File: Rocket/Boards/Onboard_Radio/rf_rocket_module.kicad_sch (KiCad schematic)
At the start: 13 parts

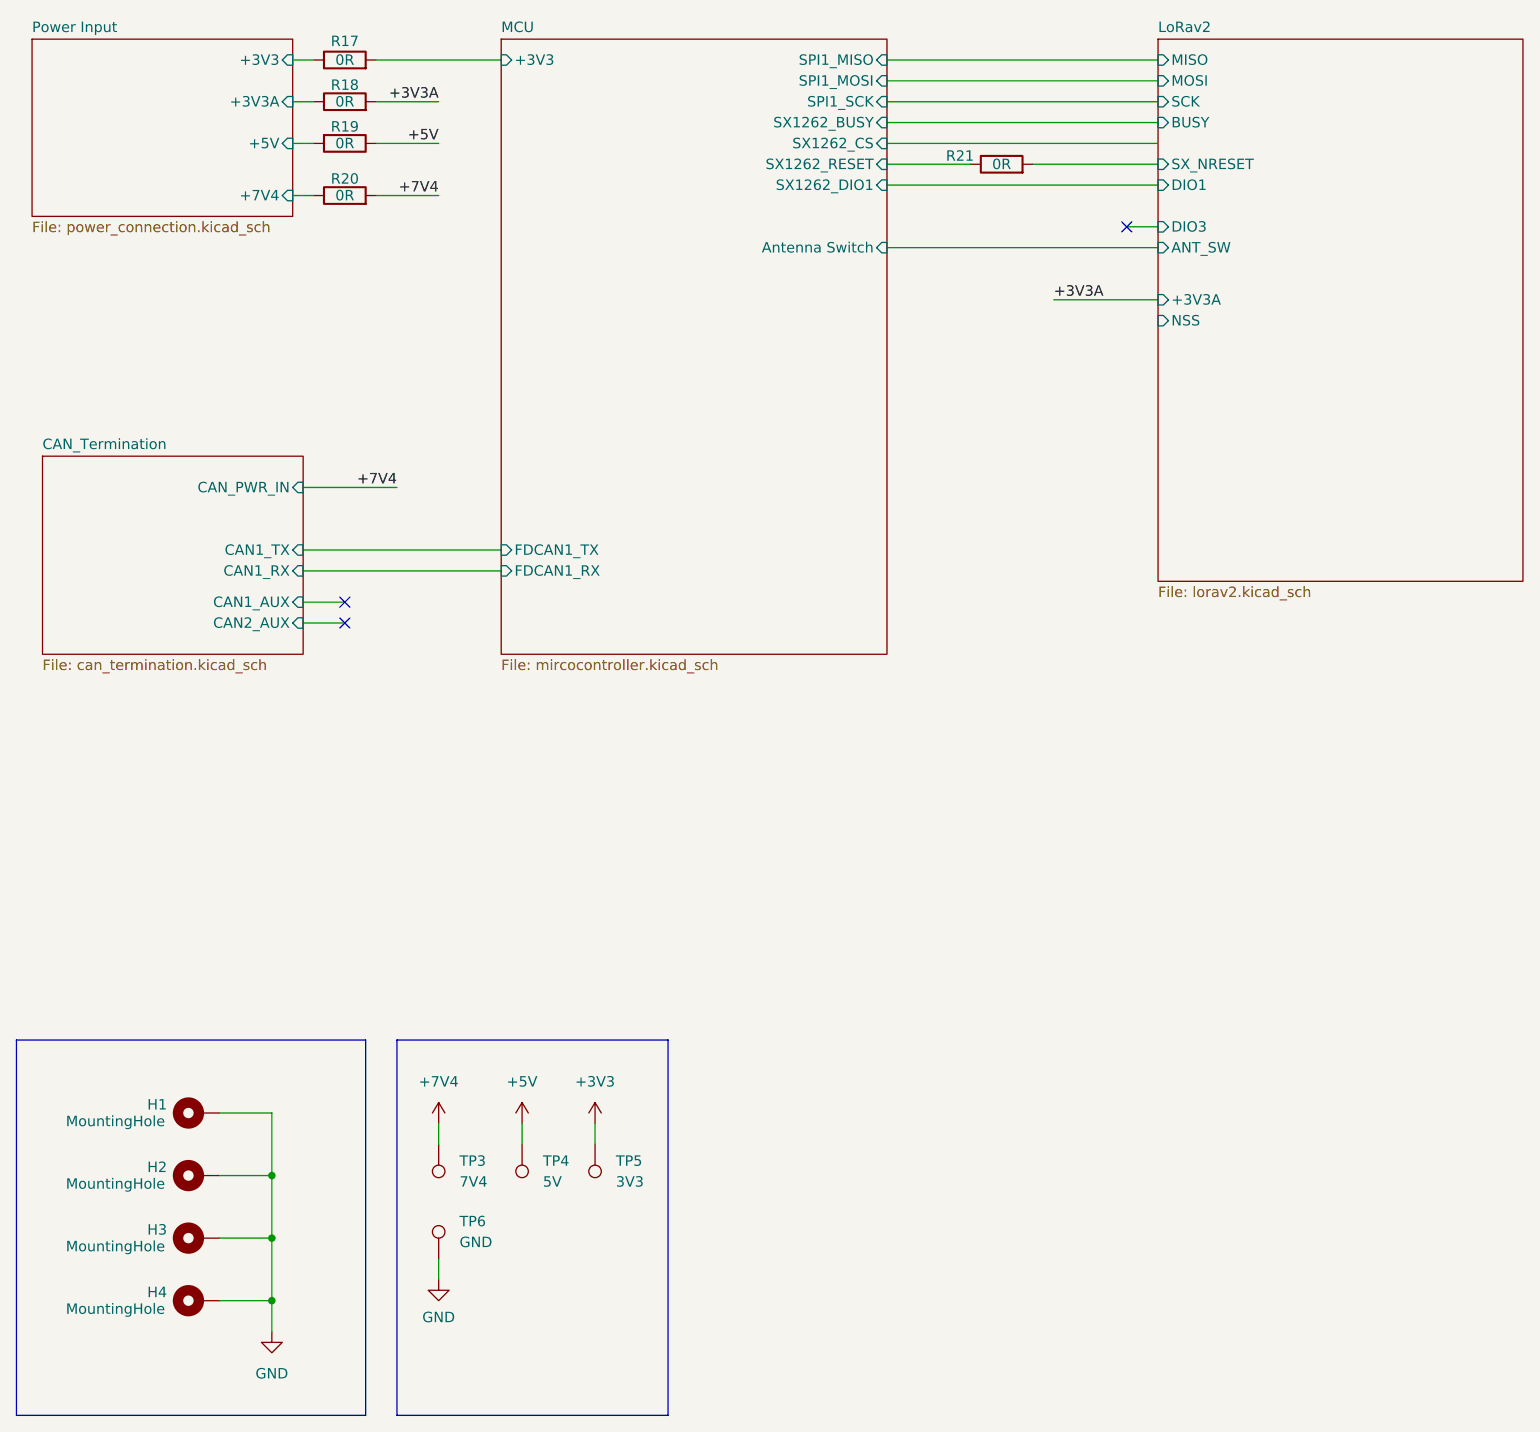
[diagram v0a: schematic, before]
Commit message: can bus updeated
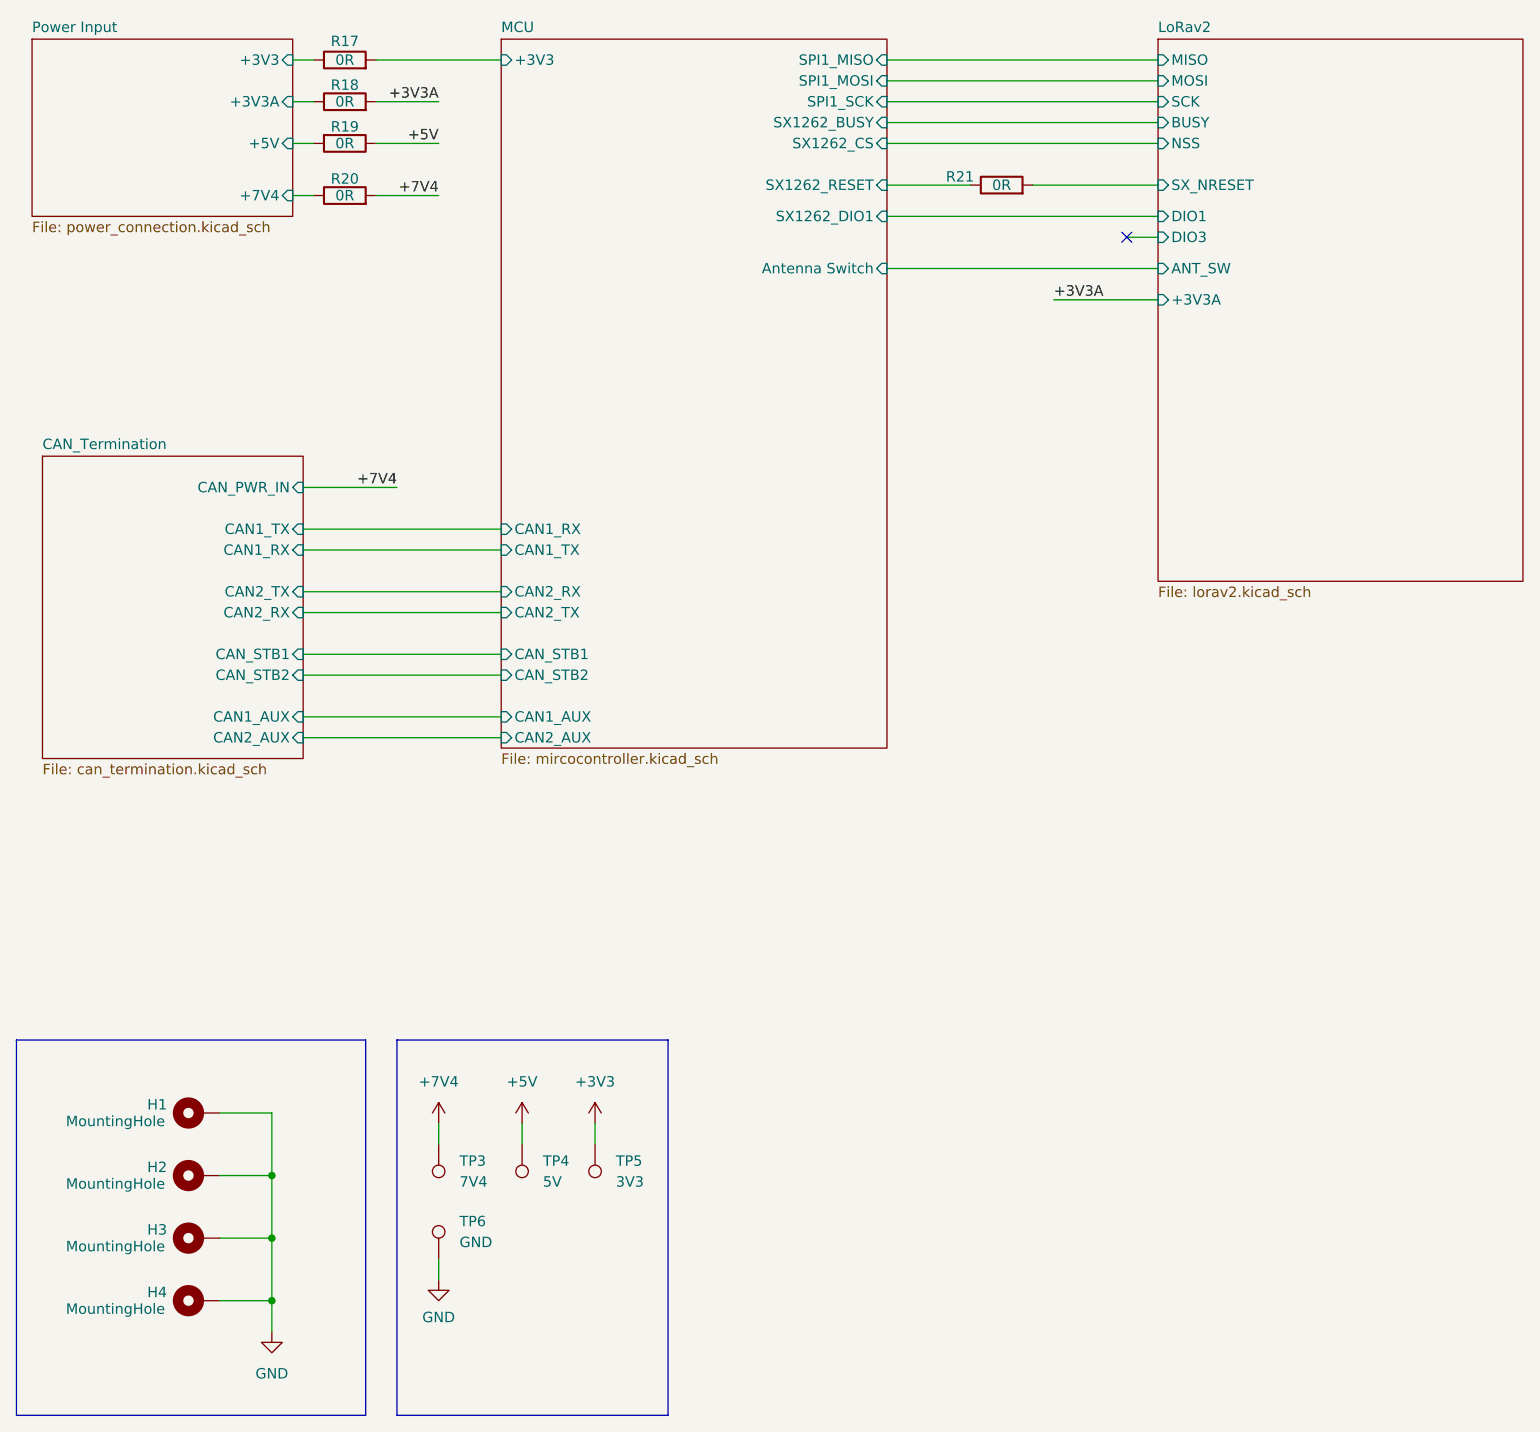
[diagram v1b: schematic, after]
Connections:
- no-connect marks 3 -> 1
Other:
- sheet CAN_Termination ports: added CAN2_RX, CAN2_TX, CAN_STB1, CAN_STB2; removed none
- sheet MCU ports: added CAN1_AUX, CAN1_RX, CAN1_TX, CAN2_AUX, CAN2_RX, CAN2_TX, CAN_STB1, CAN_STB2; removed FDCAN1_RX, FDCAN1_TX
- title: (none) -> Onboard Radio
- moved on the sheet: R21
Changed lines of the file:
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@@
 	(generator_version "10.0")
 	(paper "A4")
+	(title_block
+		(title "Onboard Radio")
+		(date "2026-05-28")
+		(rev "A")
+	)
 	(rectangle
 		(start 18.415 142.24)
@@
 	)
 	(no_connect
-		(at 58.42 88.9)
-	)
-	(no_connect
-		(at 153.67 43.18)
-	)
-	(no_connect
-		(at 58.42 91.44)
+		(at 153.67 44.45)
 	)
 	(wire
@@
 	(wire
 		(pts
+			(xy 53.34 87.63) (xy 77.47 87.63)
+		)
+		(stroke
+			(width 0)
+			(type default)
+		)
+	)
+	(wire
+		(pts
 			(xy 124.46 22.86) (xy 157.48 22.86)
 		)
@@
 	(wire
 		(pts
-			(xy 153.67 43.18) (xy 157.48 43.18)
+			(xy 53.34 95.25) (xy 77.47 95.25)
 		)
 		(stroke
@@
 	(wire
 		(pts
-			(xy 53.34 82.55) (xy 77.47 82.55)
+			(xy 53.34 80.01) (xy 77.47 80.01)
 		)
 		(stroke
@@
 	(wire
 		(pts
-			(xy 144.78 52.07) (xy 157.48 52.07)
+			(xy 124.46 38.1) (xy 134.62 38.1)
 		)
 		(stroke
@@
 	(wire
 		(pts
-			(xy 124.46 45.72) (xy 157.48 45.72)
+			(xy 144.78 52.07) (xy 157.48 52.07)
 		)
 		(stroke
@@
 	(wire
 		(pts
-			(xy 124.46 35.56) (xy 134.62 35.56)
+			(xy 153.67 44.45) (xy 157.48 44.45)
+		)
+		(stroke
+			(width 0)
+			(type default)
+		)
+	)
+	(wire
+		(pts
+			(xy 142.24 38.1) (xy 157.48 38.1)
 		)
 		(stroke
@@
 	(wire
 		(pts
+			(xy 53.34 97.79) (xy 77.47 97.79)
+		)
+		(stroke
+			(width 0)
+			(type default)
+		)
+	)
+	(wire
+		(pts
 			(xy 43.18 166.37) (xy 49.53 166.37)
 		)
@@
 	(wire
 		(pts
-			(xy 53.34 88.9) (xy 58.42 88.9)
+			(xy 53.34 102.87) (xy 77.47 102.87)
 		)
 		(stroke
@@
 	(wire
 		(pts
+			(xy 53.34 90.17) (xy 77.47 90.17)
+		)
+		(stroke
+			(width 0)
+			(type default)
+		)
+	)
+	(wire
+		(pts
 			(xy 54.61 22.86) (xy 52.07 22.86)
 		)
@@
 	(wire
 		(pts
-			(xy 142.24 35.56) (xy 157.48 35.56)
+			(xy 124.46 48.26) (xy 157.48 48.26)
 		)
 		(stroke
@@
 	(wire
 		(pts
-			(xy 53.34 91.44) (xy 58.42 91.44)
+			(xy 53.34 105.41) (xy 77.47 105.41)
 		)
 		(stroke
@@
 	(wire
 		(pts
-			(xy 124.46 38.1) (xy 157.48 38.1)
+			(xy 124.46 41.91) (xy 157.48 41.91)
 		)
 		(stroke
@@
 	(wire
 		(pts
-			(xy 53.34 85.09) (xy 77.47 85.09)
+			(xy 53.34 82.55) (xy 77.47 82.55)
 		)
 		(stroke
@@
 	(symbol
 		(lib_id "Device:R")
-		(at 138.43 35.56 90)
+		(at 138.43 38.1 90)
 		(unit 1)
 		(body_style 1)
@@
 		(dnp no)
 		(property "Reference" "R21"
-			(at 133.35 34.544 90)
+			(at 133.35 37.084 90)
 			(show_name no)
 			(do_not_autoplace no)
@@
 		)
 		(property "Value" "0R"
-			(at 138.43 35.56 90)
+			(at 138.43 38.1 90)
 			(show_name no)
 			(do_not_autoplace no)
@@
 		)
 		(property "Footprint" "Resistor_SMD:R_0603_1608Metric"
-			(at 138.43 37.338 90)
+			(at 138.43 39.878 90)
 			(hide yes)
 			(show_name no)
@@
 		)
 		(property "Datasheet" ""
-			(at 138.43 35.56 0)
+			(at 138.43 38.1 0)
 			(hide yes)
 			(show_name no)
@@
 		)
 		(property "Description" "Resistor"
-			(at 138.43 35.56 0)
+			(at 138.43 38.1 0)
 			(hide yes)
 			(show_name no)
@@
 		)
 		(property "KLC_S3.3" ""
-			(at 138.43 35.56 90)
+			(at 138.43 38.1 90)
 			(hide yes)
 			(show_name no)
@@
 		)
 		(property "KLC_S4.1" ""
-			(at 138.43 35.56 90)
+			(at 138.43 38.1 90)
 			(hide yes)
 			(show_name no)
@@
 	(sheet
 		(at 77.47 20.32)
-		(size 46.99 74.93)
+		(size 46.99 86.36)
 		(exclude_from_sim no)
 		(in_bom yes)
@@
 		)
 		(property "Sheetfile" "mircocontroller.kicad_sch"
-			(at 77.47 95.8346 0)
+			(at 77.47 107.2646 0)
 			(show_name no)
 			(do_not_autoplace no)
@@
 			)
 		)
-		(pin "FDCAN1_RX" input
-			(at 77.47 85.09 180)
-			(effects
-				(font
-					(size 1.27 1.27)
-				)
-				(justify left)
-			)
-		)
-		(pin "FDCAN1_TX" input
-			(at 77.47 82.55 180)
-			(effects
-				(font
-					(size 1.27 1.27)
-				)
-				(justify left)
-			)
-		)
 		(pin "SPI1_MISO" input
 			(at 124.46 22.86 0)
@@
 		)
 		(pin "SX1262_DIO1" input
-			(at 124.46 38.1 0)
+			(at 124.46 41.91 0)
 			(effects
 				(font
@@
 		)
 		(pin "SX1262_RESET" input
-			(at 124.46 35.56 0)
+			(at 124.46 38.1 0)
 			(effects
 				(font
@@
 		)
 		(pin "Antenna Switch" input
-			(at 124.46 45.72 0)
+			(at 124.46 48.26 0)
 			(effects
 				(font
@@
 			)
 		)
+		(pin "CAN1_AUX" input
+			(at 77.47 102.87 180)
+			(effects
+				(font
+					(size 1.27 1.27)
+				)
+				(justify left)
+			)
+		)
+		(pin "CAN2_AUX" input
+			(at 77.47 105.41 180)
+			(effects
+				(font
+					(size 1.27 1.27)
+				)
+				(justify left)
+			)
+		)
+		(pin "CAN1_RX" input
+			(at 77.47 80.01 180)
+			(effects
+				(font
+					(size 1.27 1.27)
+				)
+				(justify left)
+			)
+		)
+		(pin "CAN1_TX" input
+			(at 77.47 82.55 180)
+			(effects
+				(font
+					(size 1.27 1.27)
+				)
+				(justify left)
+			)
+		)
+		(pin "CAN2_RX" input
+			(at 77.47 87.63 180)
+			(effects
+				(font
+					(size 1.27 1.27)
+				)
+				(justify left)
+			)
+		)
+		(pin "CAN2_TX" input
+			(at 77.47 90.17 180)
+			(effects
+				(font
+					(size 1.27 1.27)
+				)
+				(justify left)
+			)
+		)
+		(pin "CAN_STB1" input
+			(at 77.47 95.25 180)
+			(effects
+				(font
+					(size 1.27 1.27)
+				)
+				(justify left)
+			)
+		)
+		(pin "CAN_STB2" input
+			(at 77.47 97.79 180)
+			(effects
+				(font
+					(size 1.27 1.27)
+				)
+				(justify left)
+			)
+		)
 		(instances
 			(project "rf_rocket_module"
@@
 	(sheet
 		(at 21.59 71.12)
-		(size 31.75 24.13)
+		(size 31.75 36.83)
 		(exclude_from_sim no)
 		(in_bom yes)
@@
 		)
 		(property "Sheetfile" "can_termination.kicad_sch"
-			(at 21.59 95.8346 0)
+			(at 21.59 108.5346 0)
 			(show_name no)
 			(do_not_autoplace no)
@@
 		)
 		(pin "CAN1_RX" input
-			(at 53.34 85.09 0)
+			(at 53.34 82.55 0)
 			(effects
 				(font
@@
 		)
 		(pin "CAN1_TX" input
-			(at 53.34 82.55 0)
+			(at 53.34 80.01 0)
 			(effects
 				(font
@@
 		)
 		(pin "CAN1_AUX" input
-			(at 53.34 88.9 0)
+			(at 53.34 102.87 0)
 			(effects
 				(font
@@
 		)
 		(pin "CAN2_AUX" input
-			(at 53.34 91.44 0)
+			(at 53.34 105.41 0)
 			(effects
 				(font
@@
 			)
 		)
+		(pin "CAN2_RX" input
+			(at 53.34 90.17 0)
+			(effects
+				(font
+					(size 1.27 1.27)
+				)
+				(justify right)
+			)
+		)
+		(pin "CAN2_TX" input
+			(at 53.34 87.63 0)
+			(effects
+				(font
+					(size 1.27 1.27)
+				)
+				(justify right)
+			)
+		)
+		(pin "CAN_STB1" input
+			(at 53.34 95.25 0)
+			(effects
+				(font
+					(size 1.27 1.27)
+				)
+				(justify right)
+			)
+		)
+		(pin "CAN_STB2" input
+			(at 53.34 97.79 0)
+			(effects
+				(font
+					(size 1.27 1.27)
+				)
+				(justify right)
+			)
+		)
 		(instances
 			(project "rf_rocket_module"
@@
 		)
 		(pin "DIO3" input
-			(at 157.48 43.18 180)
+			(at 157.48 44.45 180)
 			(effects
 				(font
@@
 		)
 		(pin "DIO1" input
-			(at 157.48 38.1 180)
+			(at 157.48 41.91 180)
 			(effects
 				(font
@@
 		)
 		(pin "ANT_SW" input
-			(at 157.48 45.72 180)
+			(at 157.48 48.26 180)
 			(effects
 				(font
@@
 			)
 		)
-		(pin "NSS" input
-			(at 157.48 54.61 180)
+		(pin "SX_NRESET" input
+			(at 157.48 38.1 180)
 			(effects
 				(font
@@
 			)
 		)
-		(pin "SX_NRESET" input
-			(at 157.48 35.56 180)
+		(pin "NSS" input
+			(at 157.48 33.02 180)
 			(effects
 				(font

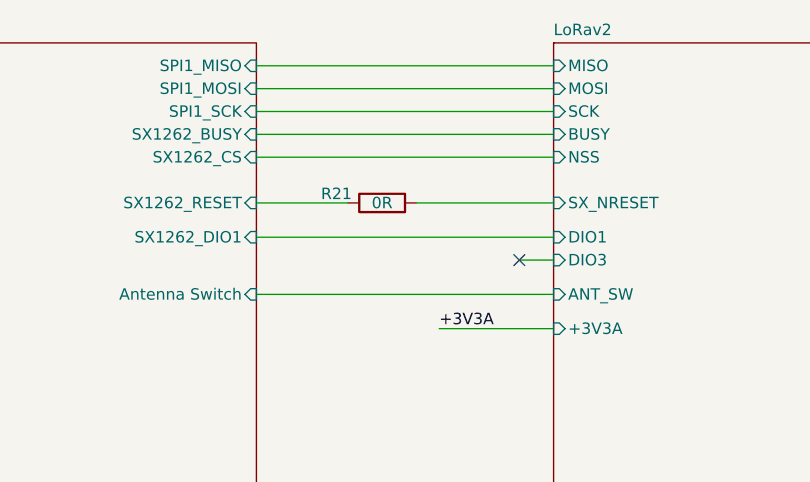
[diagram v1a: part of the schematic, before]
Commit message: radio ic board planes joined, pcb made smaller, need to add cantraces before review
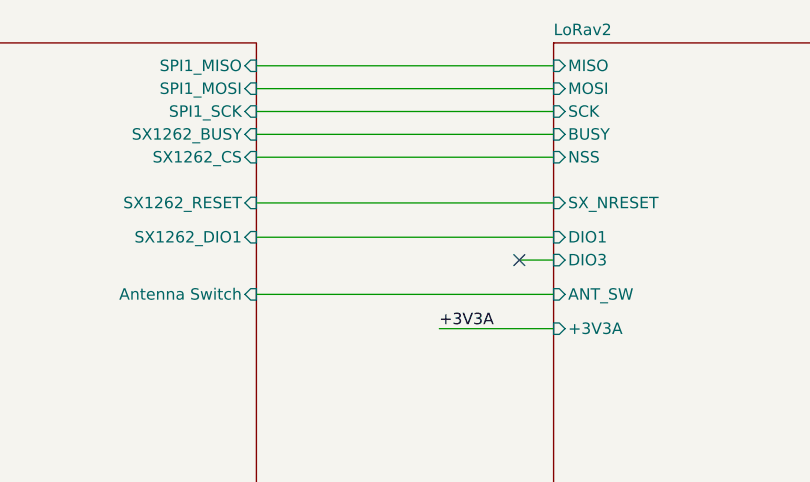
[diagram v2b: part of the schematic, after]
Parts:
- removed R21: 0R, Resistor_SMD:R_0603_1608Metric, symbol Device:R
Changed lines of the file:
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@@
 	(wire
 		(pts
-			(xy 124.46 38.1) (xy 134.62 38.1)
+			(xy 124.46 38.1) (xy 157.48 38.1)
 		)
 		(stroke
@@
 		(pts
 			(xy 153.67 44.45) (xy 157.48 44.45)
-		)
-		(stroke
-			(width 0)
-			(type default)
-		)
-	)
-	(wire
-		(pts
-			(xy 142.24 38.1) (xy 157.48 38.1)
 		)
 		(stroke
@@
 	)
 	(symbol
-		(lib_id "Device:R")
-		(at 138.43 38.1 90)
-		(unit 1)
-		(body_style 1)
-		(exclude_from_sim no)
-		(in_bom yes)
-		(on_board yes)
-		(in_pos_files yes)
-		(dnp no)
-		(property "Reference" "R21"
-			(at 133.35 37.084 90)
-			(show_name no)
-			(do_not_autoplace no)
-			(effects
-				(font
-					(size 1.27 1.27)
-				)
-			)
-		)
-		(property "Value" "0R"
-			(at 138.43 38.1 90)
-			(show_name no)
-			(do_not_autoplace no)
-			(effects
-				(font
-					(size 1.27 1.27)
-				)
-			)
-		)
-		(property "Footprint" "Resistor_SMD:R_0603_1608Metric"
-			(at 138.43 39.878 90)
-			(hide yes)
-			(show_name no)
-			(do_not_autoplace no)
-			(effects
-				(font
-					(size 1.27 1.27)
-				)
-			)
-		)
-		(property "Datasheet" ""
-			(at 138.43 38.1 0)
-			(hide yes)
-			(show_name no)
-			(do_not_autoplace no)
-			(effects
-				(font
-					(size 1.27 1.27)
-				)
-			)
-		)
-		(property "Description" "Resistor"
-			(at 138.43 38.1 0)
-			(hide yes)
-			(show_name no)
-			(do_not_autoplace no)
-			(effects
-				(font
-					(size 1.27 1.27)
-				)
-			)
-		)
-		(property "KLC_S3.3" ""
-			(at 138.43 38.1 90)
-			(hide yes)
-			(show_name no)
-			(do_not_autoplace no)
-			(effects
-				(font
-					(size 1.27 1.27)
-				)
-			)
-		)
-		(property "KLC_S4.1" ""
-			(at 138.43 38.1 90)
-			(hide yes)
-			(show_name no)
-			(do_not_autoplace no)
-			(effects
-				(font
-					(size 1.27 1.27)
-				)
-			)
-		)
-		(pin "1"
-		)
-		(pin "2"
-		)
-		(instances
-			(project "rf_rocket_module"
-				(path "/4940ffbe-f45f-4917-a247-12e2b32b6c35"
-					(reference "R21")
-					(unit 1)
-				)
-			)
-		)
-	)
-	(symbol
 		(lib_id "power:+7.5V")
 		(at 69.85 152.4 0)
@@
 		(exclude_from_sim no)
 		(in_bom no)
-		(on_board yes)
+		(on_board no)
 		(in_pos_files yes)
 		(dnp no)
@@
 		(exclude_from_sim no)
 		(in_bom no)
-		(on_board yes)
+		(on_board no)
 		(in_pos_files yes)
 		(dnp no)
@@
 		(exclude_from_sim no)
 		(in_bom no)
-		(on_board yes)
+		(on_board no)
 		(in_pos_files yes)
 		(dnp no)
@@
 		(exclude_from_sim no)
 		(in_bom no)
-		(on_board yes)
+		(on_board no)
 		(in_pos_files yes)
 		(dnp no)
